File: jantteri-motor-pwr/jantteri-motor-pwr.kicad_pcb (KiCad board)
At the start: 2 copper layers, 40 x 90.2 mm, 55 parts, among them J1 Conn_01x06_Male, J2 SWD, J3 DBG, J4 POT, J5 12V, J6 PWR-SW, J7 M, Q1 PDN3909S, Q2 IRLML6402TRPBF, Q3 IRLML6402TRPBF, U1 lora-mod, U2 STM32G030C8T6, U3 AP2301, U4 AMS1117-3.3, U5 AP2301, U6 LM2596S-5, U7 DRV8848, Y1 16MHz

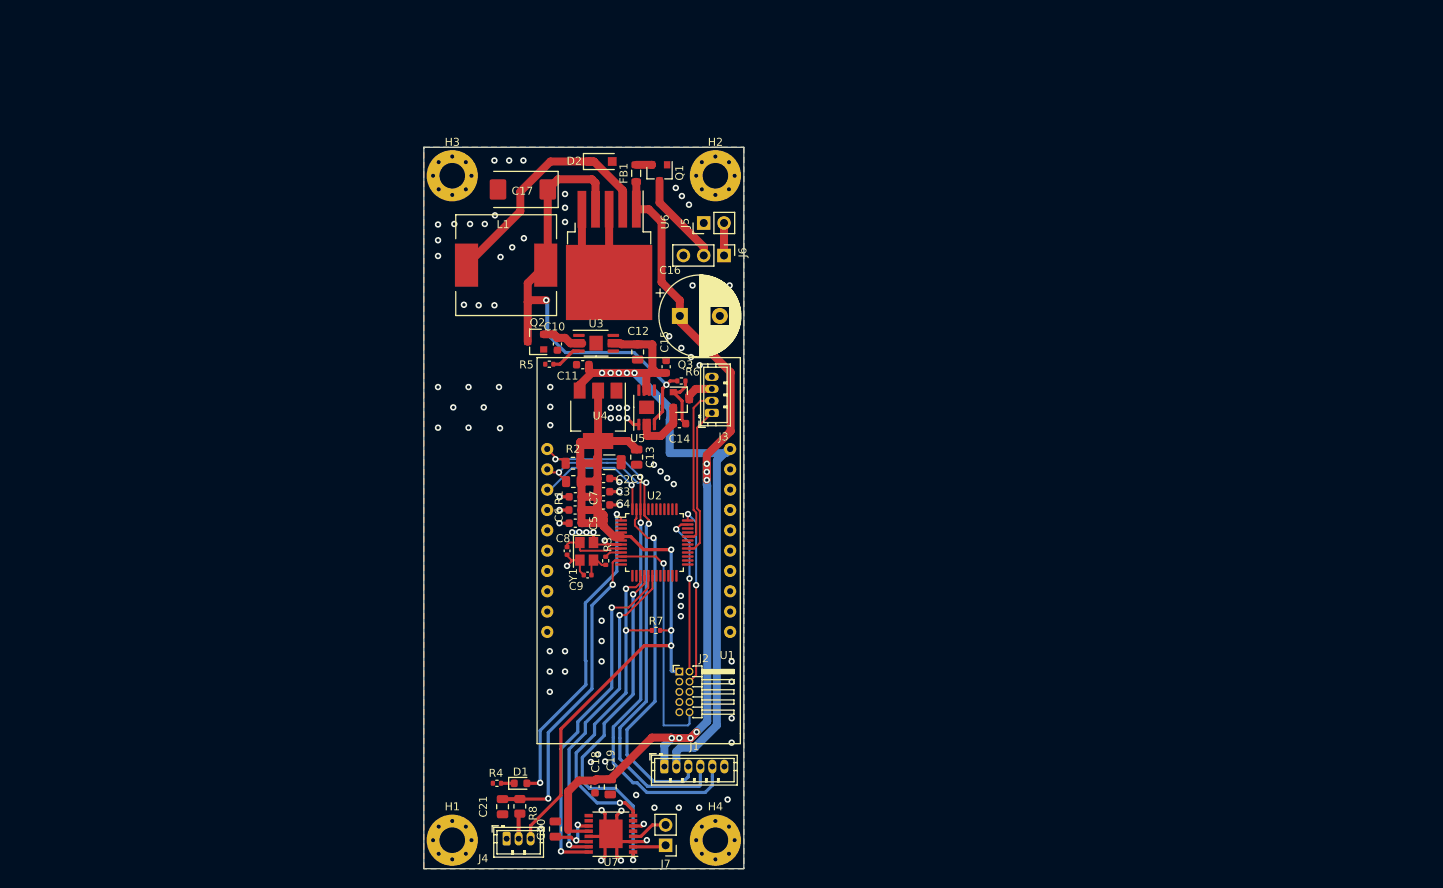
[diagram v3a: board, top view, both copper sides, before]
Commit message: Tuubijantteri design Ordered
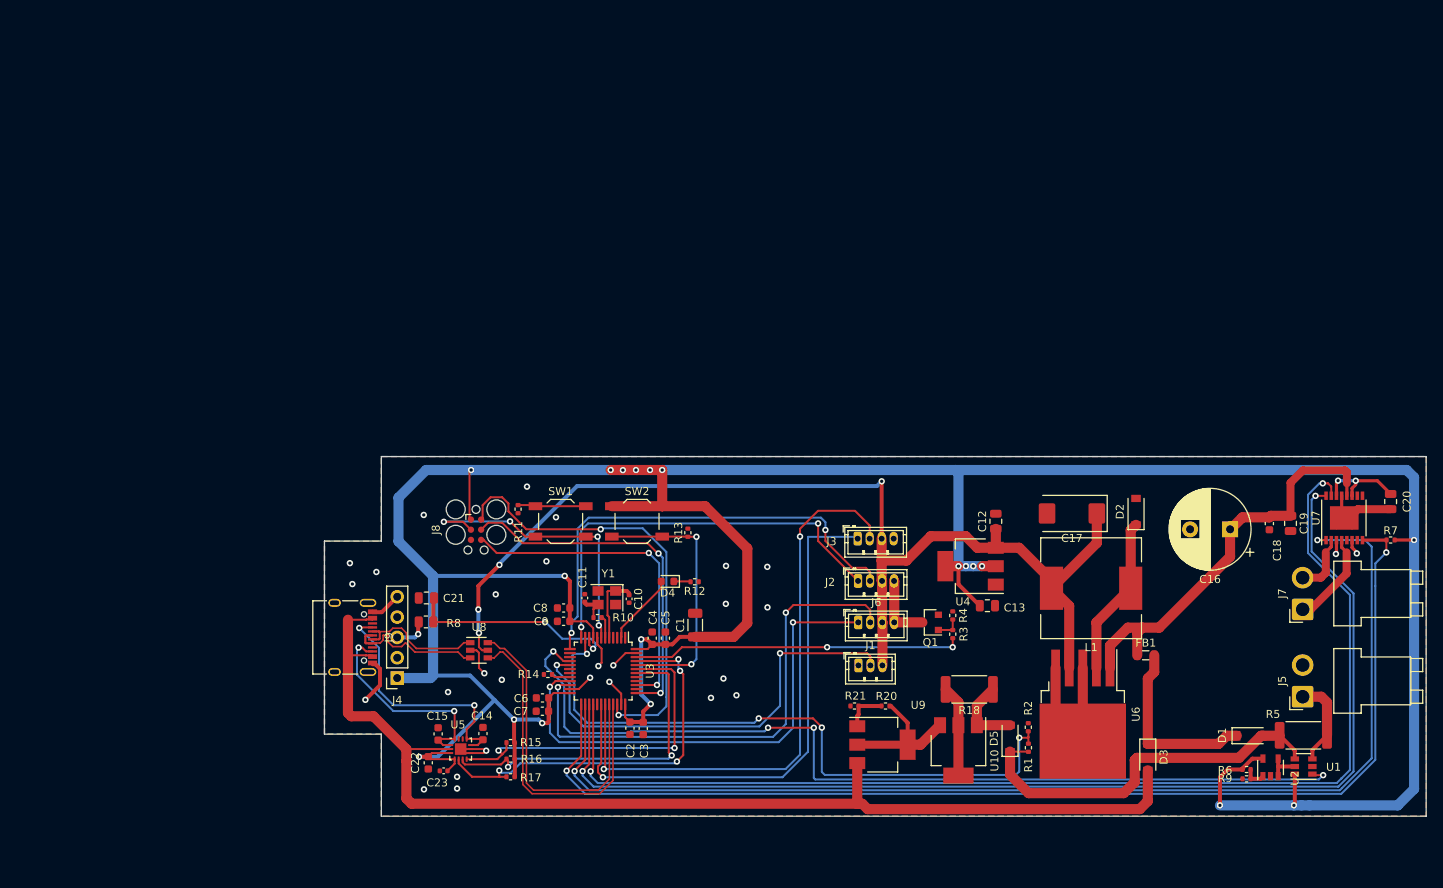
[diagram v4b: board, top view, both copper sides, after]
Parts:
- removed H1, H2, H3, H4: MountingHole_Pad, MountingHole:MountingHole_3.2mm_M3_Pad_Via
- removed Q2, Q3: IRLML6402TRPBF, Package_TO_SOT_SMD:SOT-23
- added C22: 100n, Capacitor_SMD:C_0603_1608Metric, F.Cu at (76.9, 139.7)
- added C23: 1u, Capacitor_SMD:C_0402_1005Metric, F.Cu at (78.8, 140.7)
- added D3: B5819W SL, Diode_SMD:D_SOD-123, F.Cu at (166.8, 139.0)
- added D4: LED, LED_SMD:LED_0603_1608Metric, F.Cu at (106.8, 117.0)
- added D5: B5819W SL, Diode_SMD:D_SOD-123, F.Cu at (149.6, 136.6)
- added J8: Conn_02x03_Odd_Even, Connector:Tag-Connect_TC2030-IDC-FP_2x03_P1.27mm_Vertical, F.Cu at (82.9, 110.5)
- added J9: USB_C_Receptacle_USB2.0, Connector_USB:USB_C_Receptacle_XKB_U262-16XN-4BVC11, F.Cu at (66.2, 124.0)
- added R10: 47, Resistor_SMD:R_0402_1005Metric, F.Cu at (98.0, 121.5)
- added R11: 10K, Resistor_SMD:R_0402_1005Metric, F.Cu at (88.1, 108.0)
- added R12: 1k5, Resistor_SMD:R_0402_1005Metric, F.Cu at (110.2, 117.0)
- added R13: 10K, Resistor_SMD:R_0402_1005Metric, F.Cu at (109.3, 110.9)
- added R14: 10K, Resistor_SMD:R_0402_1005Metric, F.Cu at (91.8, 128.6)
- added R15: 4K7, Resistor_SMD:R_0402_1005Metric, F.Cu at (87.2, 137.2)
- added R16: 4K7, Resistor_SMD:R_0402_1005Metric, F.Cu at (87.2, 139.2)
- added R17: 4K7, Resistor_SMD:R_0402_1005Metric, F.Cu at (87.2, 141.4)
- added R18: 5R1, Resistor_SMD:R_2512_6332Metric, F.Cu at (144.5, 130.5)
- added R20: 220, Resistor_SMD:R_0402_1005Metric, F.Cu at (134.0, 132.6)
- added R21: 2K4, Resistor_SMD:R_0402_1005Metric, F.Cu at (130.2, 132.6)
- added R9: 100K, Resistor_SMD:R_0402_1005Metric, F.Cu at (179.2, 141.7)
- added SW1: SW_SPST, Button_Switch_SMD:SW_SPST_TL3342, F.Cu at (93.4, 109.5)
- added SW2: SW_SPST, Button_Switch_SMD:SW_SPST_TL3342, F.Cu at (103.0, 109.5)
- added U10: LM317_SOT-223, Package_TO_SOT_SMD:SOT-223-3_TabPin2, F.Cu at (143.2, 138.1)
- added U8: USBLC6-2SC6, Package_TO_SOT_SMD:SOT-23-6, F.Cu at (83.2, 125.6)
- added U9: LM317_SOT-223, Package_TO_SOT_SMD:SOT-223-3_TabPin2, F.Cu at (133.7, 137.4)
- C10, C11: value 100n -> 12p; footprint Capacitor_SMD:C_0603_1608Metric -> Capacitor_SMD:C_0402_1005Metric
- C14, C15: value 100n -> 400p
- C8, C9: value 12p -> 100n; footprint Capacitor_SMD:C_0402_1005Metric -> Capacitor_SMD:C_0603_1608Metric
- D1: value LED -> B5819W SL; footprint LED_SMD:LED_0603_1608Metric -> Diode_SMD:D_SOD-123
- D2: footprint Diode_SMD:D_SOD-123F -> Diode_SMD:D_SOD-123
- J1: value Conn_01x06_Male -> LED; footprint Connector_JST2:JST_ZH_B6B-ZR_1x06_P1.50mm_Vertical -> Connector_JST2:JST_ZH_B3B-ZR_1x03_P1.50mm_Vertical
- J2: value SWD -> DBG; footprint Connector_PinHeader_1.27mm:PinHeader_2x05_P1.27mm_Horizontal -> Connector_JST2:JST_ZH_B4B-ZR_1x04_P1.50mm_Vertical
- J4: value POT -> Conn_01x05; footprint Connector_JST:JST_ZH_B3B-ZR_1x03_P1.50mm_Vertical -> Connector_PinSocket_2.54mm:PinSocket_1x05_P2.54mm_Vertical
- J5: value 12V -> BAT; footprint Connector_PinHeader_2.54mm:PinHeader_1x02_P2.54mm_Vertical -> Connector_JST2:JST_VH_B2PS-VH_1x02_P3.96mm_Horizontal
- J6: value PWR-SW -> DBG; footprint Connector_PinHeader_2.54mm:PinHeader_1x03_P2.54mm_Vertical -> Connector_JST2:JST_ZH_B4B-ZR_1x04_P1.50mm_Vertical
- J7: footprint Connector_PinHeader_2.54mm:PinHeader_1x02_P2.54mm_Vertical -> Connector_JST2:JST_VH_B2PS-VH_1x02_P3.96mm_Horizontal
- Q1: value PDN3909S -> AO3400A
- R1: value 4K7 -> 150K; footprint Resistor_SMD:R_0805_2012Metric -> Resistor_SMD:R_0402_1005Metric
- R2: value 4K7 -> 15K; footprint Resistor_SMD:R_0805_2012Metric -> Resistor_SMD:R_0402_1005Metric
- R3: value 47 -> 220
- R4: value 1k5 -> 10K
- R5: value 100K -> R510; footprint Resistor_SMD:R_0402_1005Metric -> Resistor_SMD:R_2512_6332Metric
- U1: value lora-mod -> INA181; footprint voja-footprints:lora-mod -> Package_TO_SOT_SMD:SOT-23-6
- U2: value STM32G030C8T6 -> LMV321; footprint Package_QFP:LQFP-48_7x7mm_P0.5mm -> Package_TO_SOT_SMD:SOT-23-5
- U3: value AP2301 -> STM32L151C8TxA; footprint Package_SO:MSOP-8-1EP_3x3mm_P0.65mm_EP1.68x1.88mm -> Package_QFP:LQFP-48_7x7mm_P0.5mm
- U5: value AP2301 -> FUSB302BMPX; footprint Package_SO:MSOP-8-1EP_3x3mm_P0.65mm_EP1.68x1.88mm -> Package_DFN_QFN:WQFN-14-1EP_2.5x2.5mm_P0.5mm_EP1.45x1.45mm
- moved C20 112.1 mm to (197.2, 107.0), turned to 90 degrees
- moved R5 105.1 mm to (186.3, 136.2)
- moved U7 99.8 mm to (191.4, 109.1), turned to 90 degrees
- moved J5 95.5 mm to (186.2, 131.4)
- moved R7 92.5 mm to (197.2, 111.8)
- moved D1 91.4 mm to (179.6, 136.3)
- moved C19 91.2 mm to (184.7, 109.8)
- moved C18 90.5 mm to (182.0, 109.8)
- moved U1 89.0 mm to (186.3, 140.1), turned to 180 degrees
- moved FB1 87.7 mm to (166.6, 126.2), turned to 0 degrees
- moved R6 85.7 mm to (179.2, 140.5), turned to 180 degrees
- moved J7 84.9 mm to (186.2, 120.5), turned to 90 degrees
- moved L1 83.5 mm to (159.7, 117.9), turned to 180 degrees
- moved U6 82.4 mm to (158.7, 133.6)
- moved U2 82.0 mm to (182.2, 140.3), turned to 90 degrees
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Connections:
- C10 pad 1: Net-(C10-Pad1) -> /STM32L151C8T6A/HSE_IN
- C11 pad 1: +5V -> Net-(C11-Pad1)
- C14 pad 1: Net-(C14-Pad1) -> /usbc/CC1
- C15 pad 1: +5V -> /usbc/CC2
- C16 pad 1: +12V -> VIN
- C17 pad 1: /5V-buck/5V -> +5V
- C18 pad 1: +12V -> VIN
- C19 pad 1: +12V -> VIN
- C8 pad 1: /STM32G030C8T6/HSE_IN -> +3V3
- C9 pad 1: Net-(C9-Pad1) -> +3V3
- D1 pad 2: Net-(D1-Pad2) -> BAT+
- FB1 pad 1: +12V -> VIN
- FB1 pad 2: Net-(FB1-Pad2) -> Net-(D1-Pad1)
- J1 pad 1: +12V -> GND
- J1 pad 2: +5V -> LED
- J1 pad 3: HIT_INT -> +5V
- J2 pad 1: +3V3 -> /STM32L151C8T6A/PA2
- J2 pad 2: /10pinARM/SWDIO -> /STM32L151C8T6A/PA3
- J2 pad 3: GND -> +5V
- J2 pad 4: /10pinARM/SWCLK -> PERIPH_GND
- J3 pad 1: /jst-dbg/DBG_TX -> /STM32L151C8T6A/PA9
- J3 pad 2: /jst-dbg/DBG_RX -> /STM32L151C8T6A/PA10
- J3 pad 3: USB-5V -> +5V
- J4 pad 1: GND -> +3V3
- J4 pad 3: +3V3 -> Net-(J4-Pad3)
- J5 pad 1: GND -> Net-(J5-Pad1)
- J5 pad 2: Net-(J5-Pad2) -> GND
- J6 pad 1: Net-(J5-Pad2) -> /STM32L151C8T6A/PB10
- J6 pad 2: PWR+ -> /STM32L151C8T6A/PB11
- J6 pad 3: GND -> +5V
- J7 pad 1: M- -> M+
- J7 pad 2: M+ -> M-
- L1 pad 2: /5V-buck/5V -> +5V
- Q1 pad 1: GND -> Net-(Q1-Pad1)
- Q1 pad 2: Net-(FB1-Pad2) -> GND
- Q1 pad 3: PWR+ -> PERIPH_GND
- R1 pad 1: +3V3 -> BATMEAS
- R1 pad 2: SCL -> BAT+
- R2 pad 1: +3V3 -> GND
- R2 pad 2: SDA -> BATMEAS
- R3 pad 1: /STM32G030C8T6/HSE_OUT -> PERIPH_EN
- R3 pad 2: Net-(C9-Pad1) -> Net-(Q1-Pad1)
- R4 pad 2: Net-(D1-Pad1) -> Net-(Q1-Pad1)
- R5 pad 1: /power_protect/EN -> Net-(J5-Pad1)
- R5 pad 2: GND -> BAT+
- R6 pad 1: /5V-buck/5V -> Net-(R6-Pad1)
- R6 pad 2: GND -> +3V3
- R8 pad 2: Net-(J4-Pad2) -> Net-(J4-Pad3)
- U1 pad 1: SDA -> CURMEAS
- U1 pad 2: SCL -> GND
- U1 pad 3: LORA_INT -> Net-(J5-Pad1)
- U1 pad 4: Net-(U1-Pad4) -> BAT+
- U1 pad 6: Net-(U1-Pad6) -> +3V3
- U2 pad 1: Net-(D1-Pad2) -> Net-(R6-Pad1)
- U2 pad 2: Net-(U2-Pad2) -> GND
- U2 pad 3: Net-(U2-Pad3) -> Net-(U1-Pad5)
- U2 pad 4: +3V3 -> Net-(U1-Pad5)
- U3 pad 1: GND -> Net-(U3-Pad1)
- U3 pad 2: Net-(C10-Pad1) -> Net-(D4-Pad2)
- U3 pad 3: Net-(C10-Pad1) -> Net-(U3-Pad3)
- U3 pad 4: /power_protect/EN -> Net-(U3-Pad4)
- U3 pad 5: Net-(U3-Pad5) -> /STM32L151C8T6A/HSE_IN
- U3 pad 6: +5V -> /STM32L151C8T6A/HSE_OUT
- U3 pad 7: +5V -> /STM32L151C8T6A/NRST
- U3 pad 8: Net-(U3-Pad8) -> GND
- U3 pad 9: GND -> +3V3
- U5 pad 1: GND -> /usbc/CC2
- U5 pad 2: Net-(C14-Pad1) -> VBUS
- U5 pad 3: Net-(C14-Pad1) -> +3V3
- U5 pad 4: /5V-buck/5V -> +3V3
- U5 pad 5: Net-(U5-Pad5) -> USB_INT
- U5 pad 6: +5V -> USB_SCL
- U5 pad 7: +5V -> USB_SDA
- U5 pad 8: Net-(U5-Pad8) -> GND
- U6 pad 1: +12V -> VIN
- U6 pad 4: /5V-buck/5V -> +5V
- U7 pad 12: +12V -> VIN
- Y1 pad 1: /STM32G030C8T6/HSE_IN -> /STM32L151C8T6A/HSE_IN
- Y1 pad 3: Net-(C9-Pad1) -> Net-(C11-Pad1)
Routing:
- net +3V3: track 109.7 -> 412.8 mm, vias 3 -> 19
- net VBUS: track 0.00 -> 142.0 mm
- net CURMEAS: track 0.00 -> 116.8 mm, vias 0 -> 4
- net +12V: track 112.4 -> 0.00 mm, vias 7 -> 0
- net MOTOR_B: track 41.0 -> 146.4 mm
- net DRV_FAULT: track 42.2 -> 144.5 mm, vias 3 -> 2
- net DRV_SLEEP: track 44.7 -> 146.2 mm
- net MOTOR_A: track 43.7 -> 145.1 mm
- net BATMEAS: track 0.00 -> 80.7 mm, vias 0 -> 4
- net /STM32L151C8T6A/PA10: track 0.00 -> 73.7 mm, vias 0 -> 2
- net /STM32L151C8T6A/PA9: track 0.00 -> 70.0 mm, vias 0 -> 1
- net SDA: track 68.5 -> 0.00 mm, vias 3 -> 0
- net SCL: track 65.8 -> 0.00 mm, vias 3 -> 0
- net /STM32L151C8T6A/PB11: track 0.00 -> 63.5 mm, vias 0 -> 2
- net /STM32L151C8T6A/PB10: track 0.00 -> 61.5 mm, vias 0 -> 2
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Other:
- board size 40 x 90.2 mm -> 137.7 x 45 mm
